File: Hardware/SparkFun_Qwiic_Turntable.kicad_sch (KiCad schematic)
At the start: 5 parts

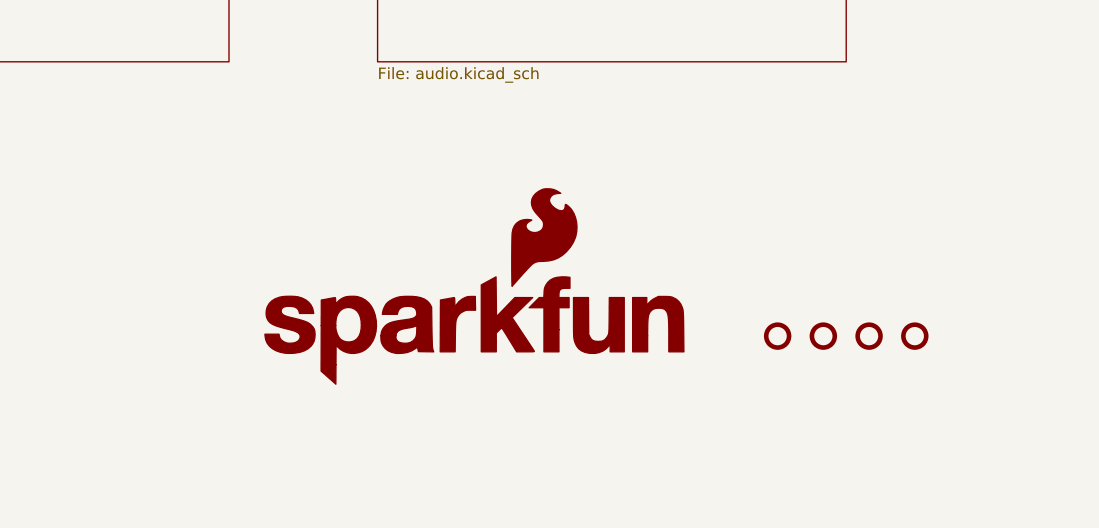
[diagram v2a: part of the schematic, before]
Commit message: Changed PCB page size to letter. Added logos to schematic.
Signed-off-by: Jamie Robertson <jrr@robertsonics.com>
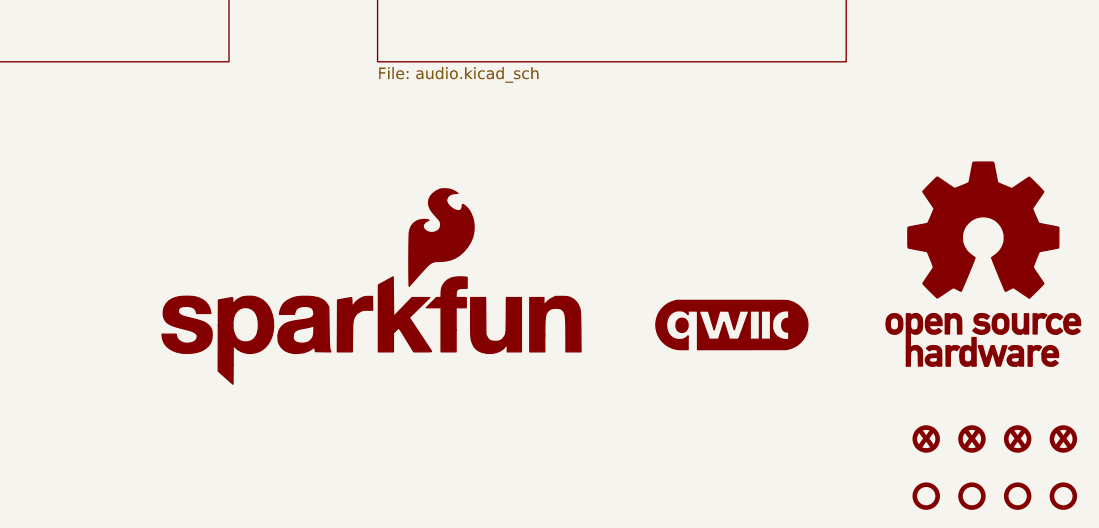
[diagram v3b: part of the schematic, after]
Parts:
- added FID1, FID2, FID3, FID4: Fiducial_0.5mm, SparkFun-Aesthetic:Fiducial_0.5mm_Mask1mm, symbol SparkFun-Aesthetic:Fiducial_0.5mm
- added G3: qwiic_Logo, symbol SparkFun-Aesthetic:qwiic_Logo
- added G4: OSHW_Logo, SparkFun-Aesthetic:Creative_Commons_License, symbol SparkFun-Aesthetic:OSHW_Logo

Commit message: Add 5V boost. Add 3.5mm jack.
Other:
- note added: "SparkFun Qwiic WAV Trigger Pro"
- note removed: "WAV Trigger Pro"
- title: WAV Trigger Pro -> SparkFun Qwiic WAV Trigger Pro
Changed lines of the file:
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@@
 	(paper "USLetter")
 	(title_block
-		(title "WAV Trigger Pro")
+		(title "SparkFun Qwiic WAV Trigger Pro")
 		(rev "1.0")
 		(company "Robertsonics / SparkFun")
@@
 		)
 	)
-	(text "WAV Trigger Pro"
+	(text "SparkFun Qwiic WAV Trigger Pro"
 		(exclude_from_sim no)
-		(at 120.904 38.354 0)
+		(at 141.224 34.29 0)
 		(effects
 			(font
 				(size 3 3)
 			)
-			(justify left bottom)
 		)
 	)
